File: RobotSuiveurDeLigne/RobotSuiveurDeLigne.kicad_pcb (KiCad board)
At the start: 2 copper layers, 108 x 48 mm, 26 parts, among them J1 US_IUT_VdA, J2 Conn_02x05_Odd_Even, U1 CNY70_IUT_VdA, U2 CNY70_IUT_VdA, U3 CNY70_IUT_VdA, U4 CNY70_IUT_VdA, U5 CNY70_IUT_VdA, U6 CNY70_IUT_VdA

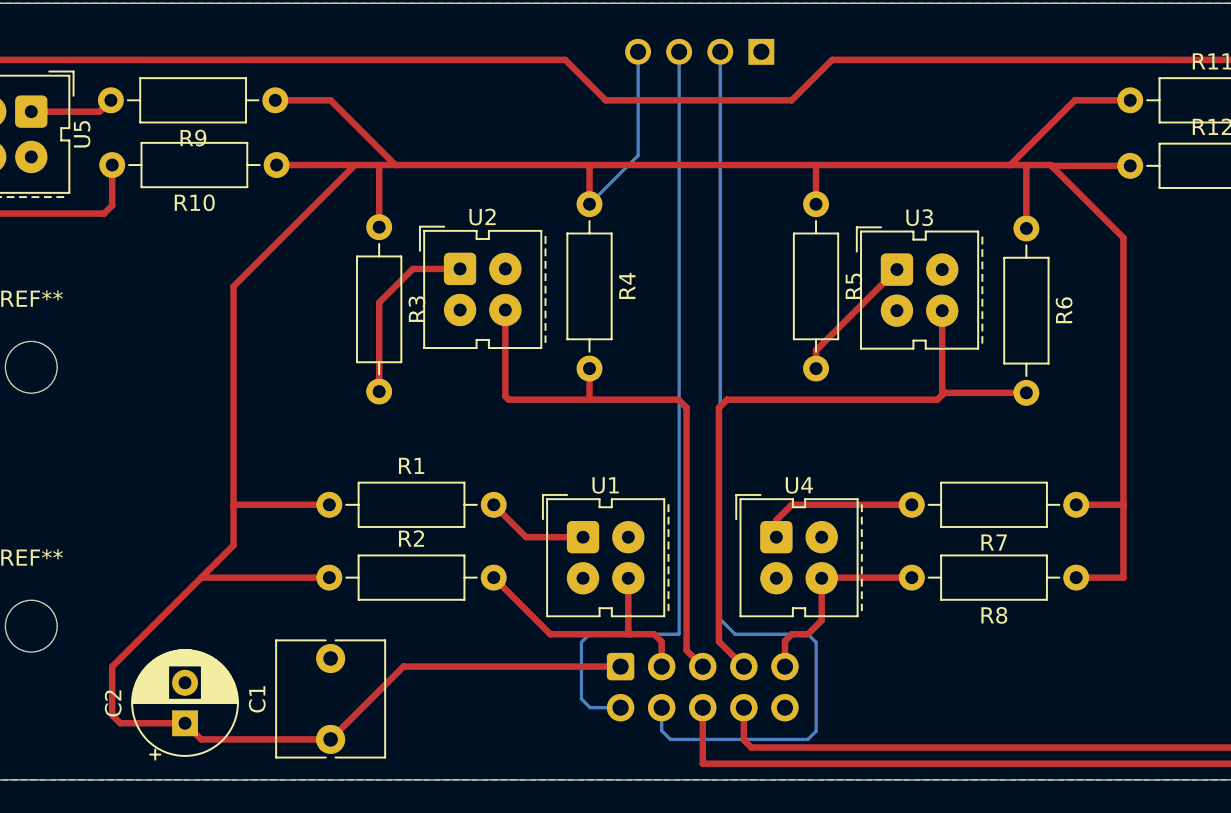
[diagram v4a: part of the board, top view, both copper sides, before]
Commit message: début de l'arrondissement des angles
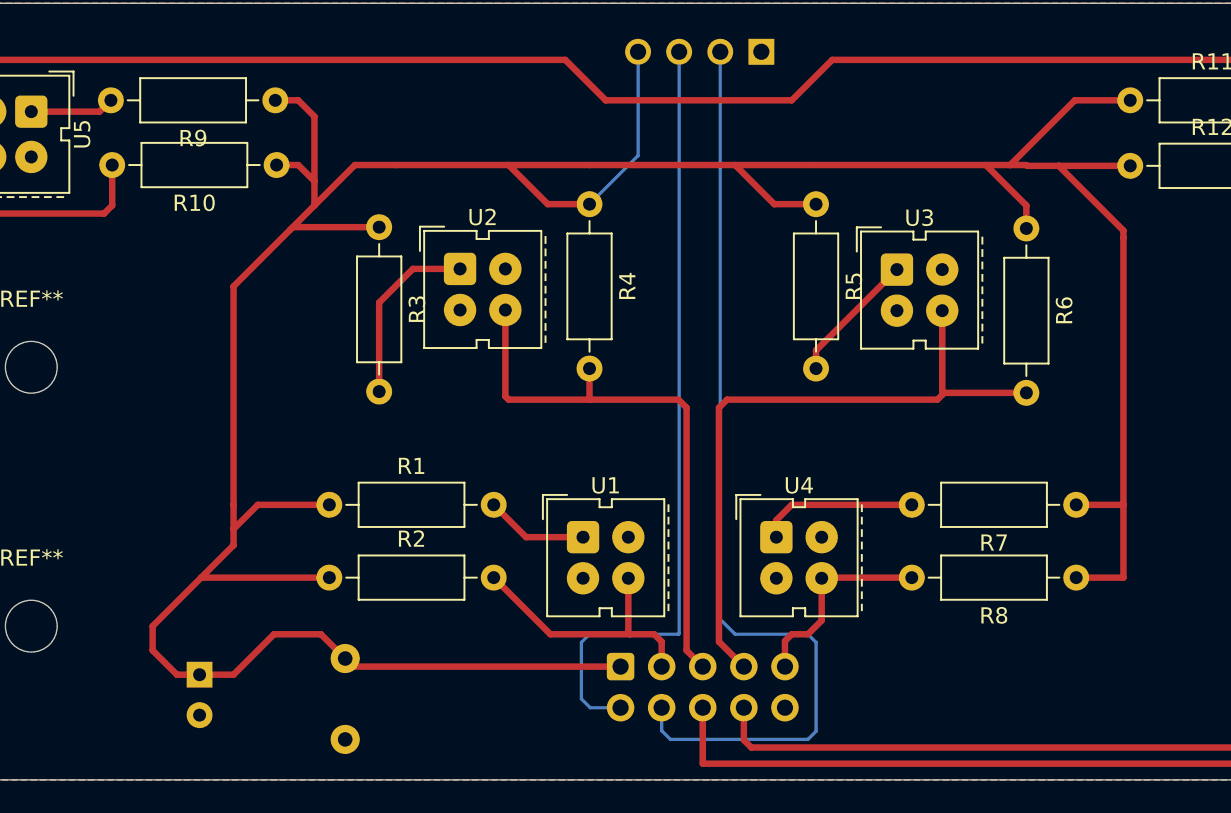
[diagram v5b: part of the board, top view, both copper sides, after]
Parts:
- C1, C2: moved to B.Cu
- moved C1 5.08 mm to (121.9, 100.5), turned to -90 degrees
- moved C2 3.13 mm to (112.9, 101.5), turned to -90 degrees

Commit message: revue complète du routage
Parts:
- moved C1 9.76 mm to (113.0, 104.5), turned to 90 degrees
- moved C2 9.32 mm to (122.0, 103.5), turned to 90 degrees
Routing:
- net Net-(J2-Pin_2): track 48.4 -> 127.9 mm
- net Net-(J2-Pin_4): track 58.5 -> 128.0 mm
- net /D1: track 107.5 -> 88.6 mm, vias 0 -> 1
- net /D0: track 224.3 -> 209.0 mm, vias 0 -> 1
- net VCC: track 215.3 -> 220.9 mm, vias 0 -> 2
- net /AN0: track 17.1 -> 20.8 mm
- net Net-(U4-A): track 9.81 -> 13.4 mm
- net GND: track 3.12 -> 0.00 mm
- net /AN1: track 35.2 -> 37.9 mm
- net Net-(U3-A): track 8.19 -> 9.92 mm
- net Net-(U2-A): track 11.4 -> 10.5 mm
- net /AN2: track 41.2 -> 41.9 mm
- net /AN3: track 12.6 -> 12.0 mm

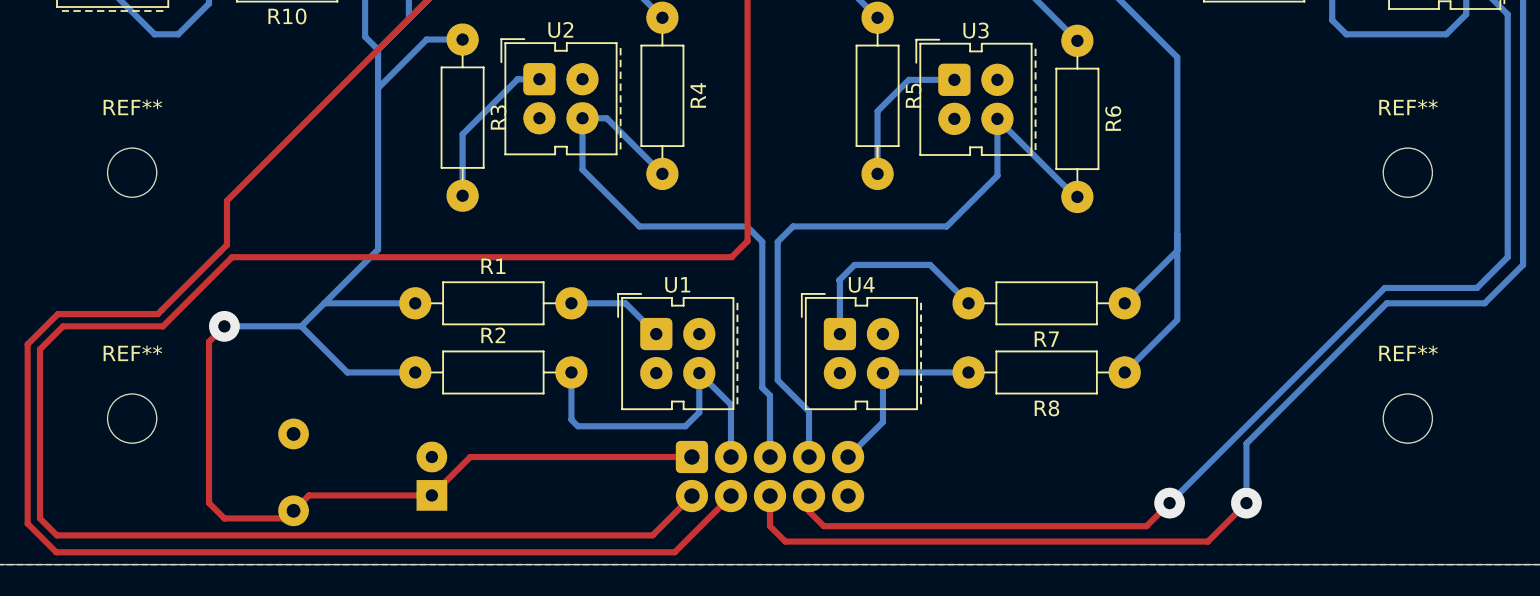
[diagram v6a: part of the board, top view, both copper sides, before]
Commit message: ajustement trous de fixation
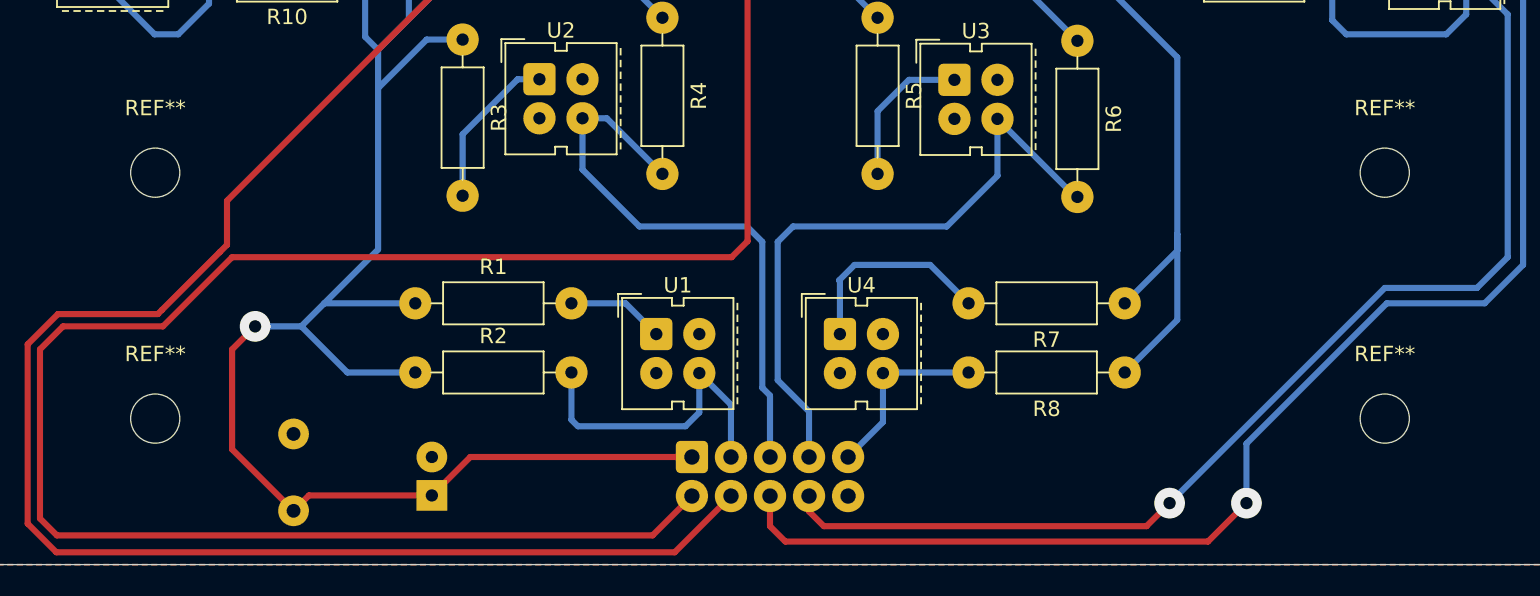
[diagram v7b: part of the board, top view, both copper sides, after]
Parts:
- moved REF** 1.50 mm to (184.0, 98.5)
- moved REF** 1.50 mm to (104.0, 98.5)
- moved REF** 1.50 mm to (184.0, 82.5)
- moved REF** 1.50 mm to (104.0, 82.5)
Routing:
- net VCC: track 220.9 -> 215.9 mm
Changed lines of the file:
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@@
 	(footprint "MountingHole:MountingHole_3.2mm_M3"
 		(layer "F.Cu")
-		(at 185.5 98.5)
+		(at 184 98.5)
 		(descr "Mounting Hole 3.2mm, no annular, M3")
 		(tags "mounting hole 3.2mm no annular m3")
@@
 	(footprint "MountingHole:MountingHole_3.2mm_M3"
 		(layer "F.Cu")
-		(at 102.5 98.5)
+		(at 104 98.5)
 		(descr "Mounting Hole 3.2mm, no annular, M3")
 		(tags "mounting hole 3.2mm no annular m3")
@@
 	(footprint "MountingHole:MountingHole_3.2mm_M3"
 		(layer "F.Cu")
-		(at 185.5 82.5)
+		(at 184 82.5)
 		(descr "Mounting Hole 3.2mm, no annular, M3")
 		(tags "mounting hole 3.2mm no annular m3")
@@
 	(footprint "MountingHole:MountingHole_3.2mm_M3"
 		(layer "F.Cu")
-		(at 102.5 82.5)
+		(at 104 82.5)
 		(descr "Mounting Hole 3.2mm, no annular, M3")
 		(tags "mounting hole 3.2mm no annular m3")
@@
 	)
 	(segment
-		(start 107.5 93.5)
-		(end 108.5 92.5)
-		(width 0.4)
-		(layer "F.Cu")
-		(net 2)
-	)
-	(segment
 		(start 113 104.5)
-		(end 112.5 105)
+		(end 109 100.5)
 		(width 0.4)
 		(layer "F.Cu")
@@
 	)
 	(segment
-		(start 108.5 105)
-		(end 107.5 104)
+		(start 109 100.5)
+		(end 109 94)
 		(width 0.4)
 		(layer "F.Cu")
@@
 	)
 	(segment
-		(start 107.5 104)
-		(end 107.5 93.5)
+		(start 113 104.5)
+		(end 112.5 105)
 		(width 0.4)
 		(layer "F.Cu")
@@
 	)
 	(segment
-		(start 112.5 105)
-		(end 108.5 105)
+		(start 109 94)
+		(end 110.5 92.5)
 		(width 0.4)
 		(layer "F.Cu")
@@
 	)
 	(via
-		(at 108.5 92.5)
+		(at 110.5 92.5)
 		(size 2)
 		(drill 0.8)
@@
 	)
 	(segment
+		(start 110.5 92.5)
+		(end 113.5 92.5)
+		(width 0.4)
+		(layer "B.Cu")
+		(net 2)
+	)
+	(segment
 		(start 170.5 87.58)
 		(end 170.5 86.5)
@@
 		(width 0.4)
 		(layer "B.Cu")
-		(net 2)
-	)
-	(segment
-		(start 108.5 92.5)
-		(end 113.5 92.5)
-		(width 0.4)
-		(layer "B.Cu")

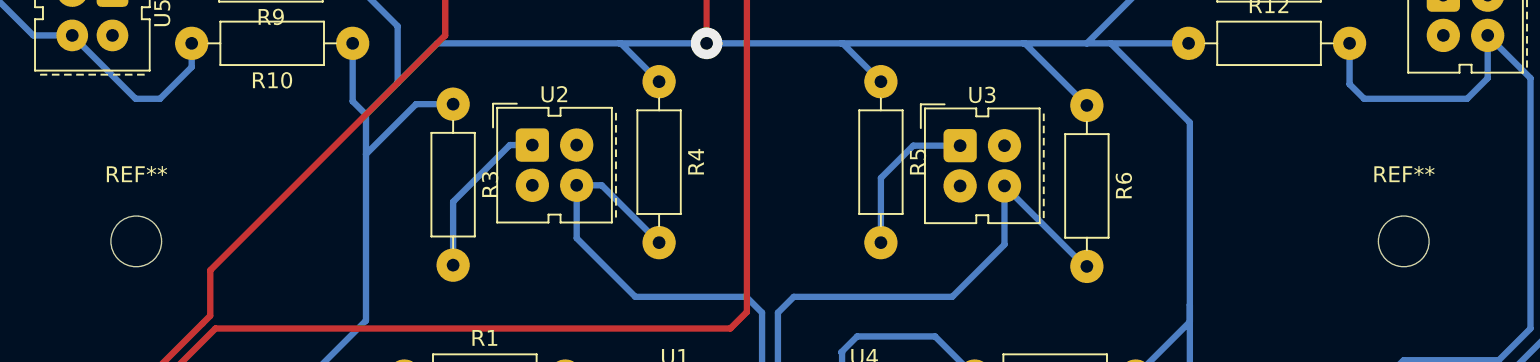
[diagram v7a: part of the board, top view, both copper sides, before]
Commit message: léger ajoustement des trous de fixation
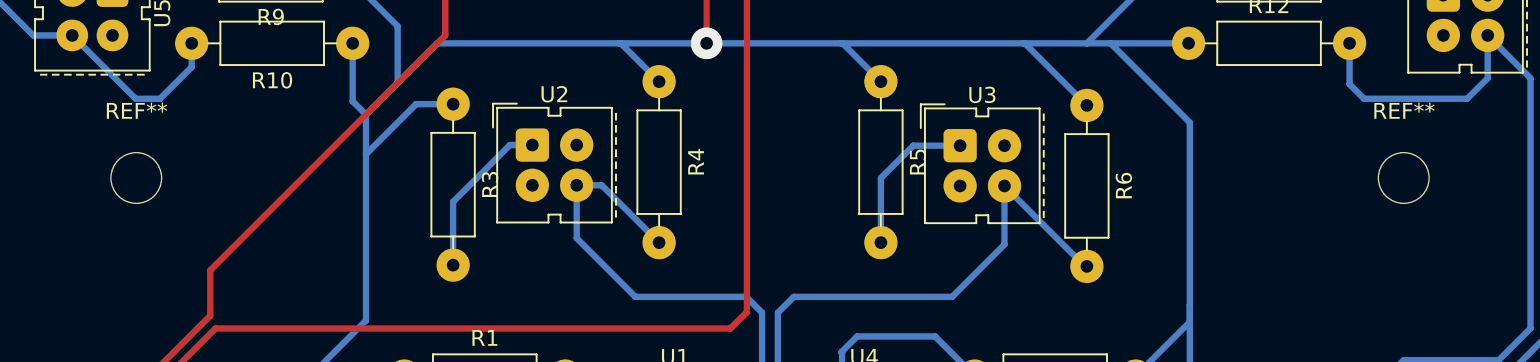
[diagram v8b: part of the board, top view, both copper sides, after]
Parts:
- moved REF** 4.00 mm to (184.0, 78.5)
- moved REF** 4.00 mm to (104.0, 78.5)
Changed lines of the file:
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@@
 	(footprint "MountingHole:MountingHole_3.2mm_M3"
 		(layer "F.Cu")
-		(at 184 82.5)
+		(at 184 78.5)
 		(descr "Mounting Hole 3.2mm, no annular, M3")
 		(tags "mounting hole 3.2mm no annular m3")
@@
 	(footprint "MountingHole:MountingHole_3.2mm_M3"
 		(layer "F.Cu")
-		(at 104 82.5)
+		(at 104 78.5)
 		(descr "Mounting Hole 3.2mm, no annular, M3")
 		(tags "mounting hole 3.2mm no annular m3")
